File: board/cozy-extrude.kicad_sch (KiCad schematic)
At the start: 8 parts, among them J1 RPi-Pico-Socket, J2 BME280, J3 PWM-Fan, J4 Screw_Terminal_01x02, J5 Screw_Terminal_01x02, K1 HF46F_5-HS1, U1 ULN2003

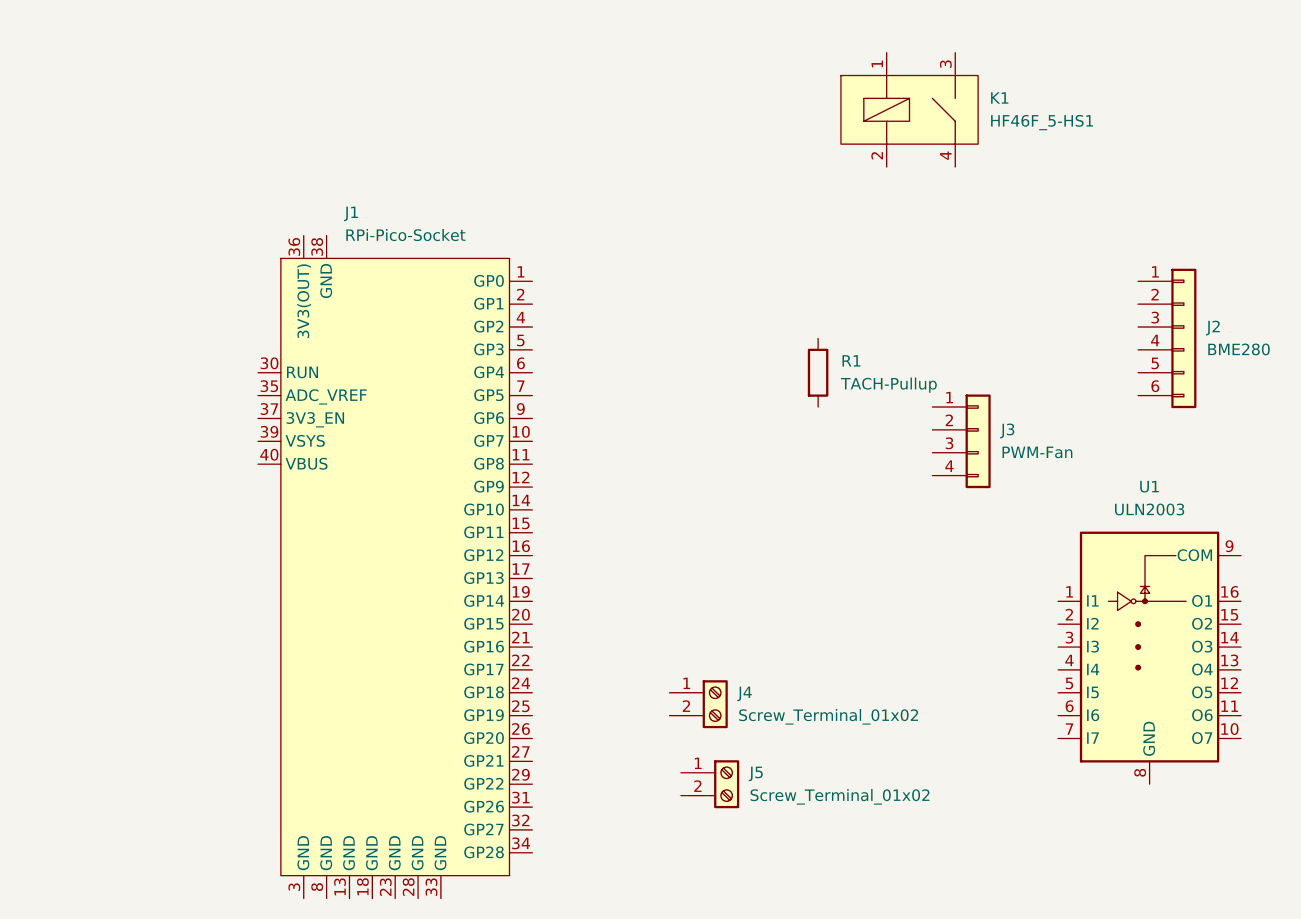
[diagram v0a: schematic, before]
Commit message: adds schematic
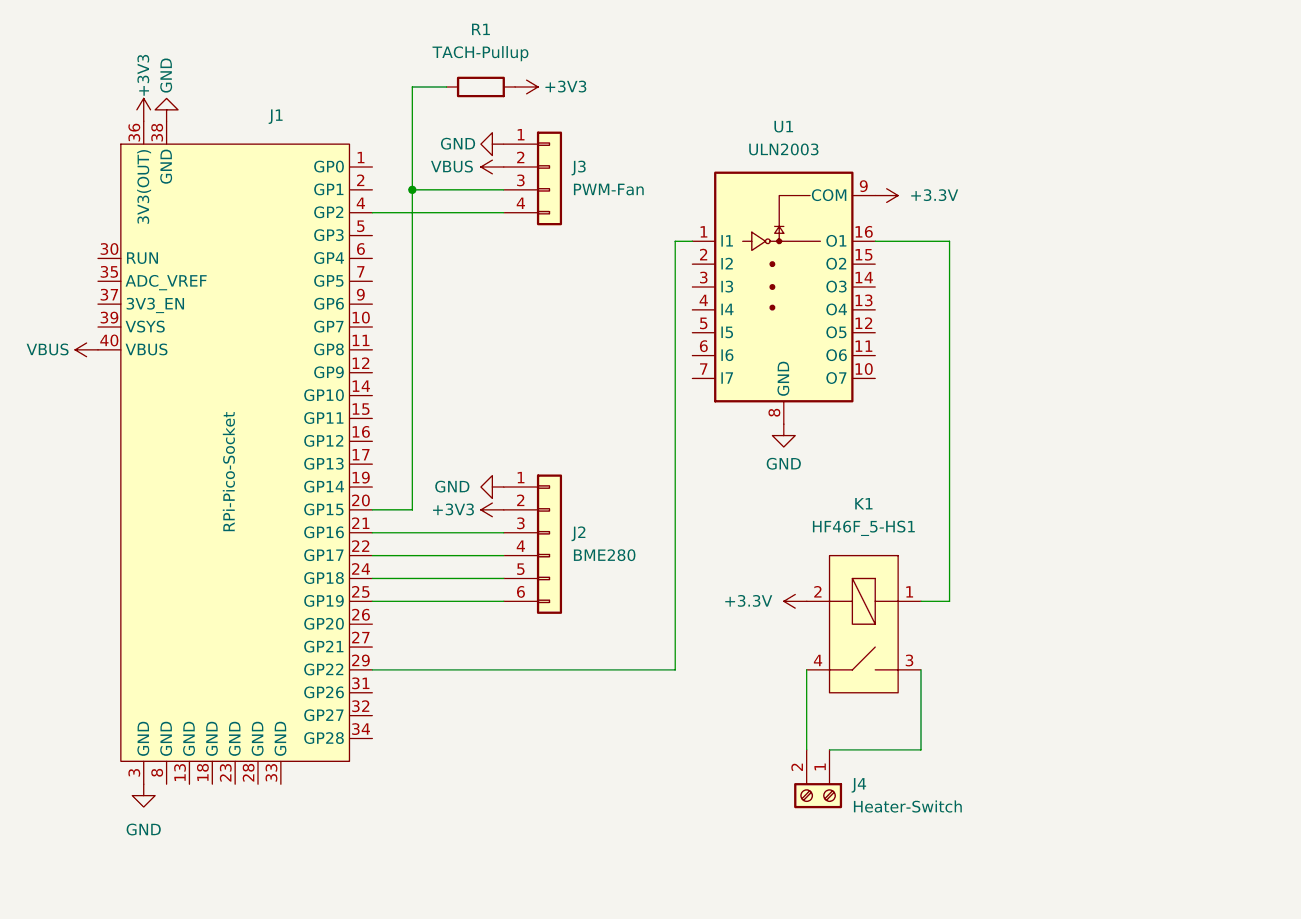
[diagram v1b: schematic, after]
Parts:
- removed J5: Screw_Terminal_01x02, TerminalBlock_Phoenix:TerminalBlock_Phoenix_MKDS-1,5-2-5.08_1x02_P5.08mm_Horizontal, symbol Connector:Screw_Terminal_01x02
- J4: value Screw_Terminal_01x02 -> Heater-Switch
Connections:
- net at J1.20 (GP15): now also J3.3 (Pin_3), R1.1
- net at J1.21 (GP16): now also J2.3 (Pin_3)
- net at J1.22 (GP17): now also J2.4 (Pin_4)
- net at J1.24 (GP18): now also J2.5 (Pin_5)
- net at J1.25 (GP19): now also J2.6 (Pin_6)
- net at J1.29 (GP22): now also U1.1 (I1)
- net GND: now reaches J1.3 (GND)
- net GND: now also J1.38 (GND), J2.1 (Pin_1), J3.1 (Pin_1), U1.8 (GND)
- net +3V3: now reaches J1.36 (3V3(OUT))
- net +3V3: now also J2.2 (Pin_2), R1.2
- net at J1.4 (GP2): now also J3.4 (Pin_4)
- net VBUS: now reaches J1.40 (VBUS)
- net VBUS: now also J3.2 (Pin_2)
- net at U1.16 (O1): now also K1.1
- net +3.3V: now reaches U1.9 (COM)
- net +3.3V: now also K1.2
- net at J4.1 (Pin_1): now also K1.3
- net at J4.2 (Pin_2): now also K1.4
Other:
- moved on the sheet: J1, J2, J3, J4, K1, R1, U1
